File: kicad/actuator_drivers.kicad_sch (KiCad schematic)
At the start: 29 parts, among them J18 Motor 12V, J19 CO2 Solenoid, J20 Chiller, K1 HF46F-12-HS1, K2 HF46F-12-HS1, Q1 IRLZ44NPBF, Q2 IRLZ44NPBF, Q3 2N7002, Q4 2N7002, Q5 IRLZ44NPBF, U10 PC817X1NIP, U11 PC817X1NIP, U3C MCP6002, U7 IR2104SPBF, U8 PC817X2NIP

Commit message: fix: Resolve 5 ERC warnings — footprints, grid alignment, net conflict
1. Inductor footprint: L_4.0x4.0mm_H2.0mm → L_Taiyo-Yuden_NR-40xx
   (power_management.kicad_sch)

2. Relay footprint (×2): Relay_SPST_HF46F → Relay_SPDT_Omron_G5V-1
   (actuator_drivers.kicad_sch — K1, K2)

3. Off-grid coordinates: TPS3823 symbol and WDT_RESET label moved
   from 300.48/310.64 to 300.99/311.15 (1.27mm grid aligned)
   PWR_FLAG reference position 28.575 → 27.94
   (power_management.kicad_sch)

4. HUM_ADC/I2C_SDA overlap: Both hierarchical labels were at same
   coordinates (55.88, 107.95). Shifted I2C_SDA and downstream
   labels down by 2.54mm each to eliminate net conflict.
   (hmi_connectors.kicad_sch)

Co-Authored-By: Devin AI <158243242+devin-ai-integration[bot]@users.noreply.github.com>
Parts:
- K1, K2: footprint Relay_THT:Relay_SPST_HF46F -> Relay_THT:Relay_SPDT_Omron_G5V-1
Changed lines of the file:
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@@
     (property "Reference" "K2" (at 104.14 91.44 0) (effects (font (size 1.27 1.27))))
     (property "Value" "HF46F-12-HS1" (at 104.14 93.98 0) (effects (font (size 1.27 1.27))))
-    (property "Footprint" "Relay_THT:Relay_SPST_HF46F" (at 104.14 101.6 0) (effects (font (size 1.27 1.27)) hide))
+    (property "Footprint" "Relay_THT:Relay_SPDT_Omron_G5V-1" (at 104.14 101.6 0) (effects (font (size 1.27 1.27)) hide))
     (property "MPN" "HF46F-12-HS1" (at 104.14 101.6 0) (effects (font (size 1.27 1.27)) hide))
     (property "Digi-Key_PN" "255-5799-ND" (at 104.14 101.6 0) (effects (font (size 1.27 1.27)) hide))
@@
     (property "Reference" "K1" (at 104.14 129.54 0) (effects (font (size 1.27 1.27))))
     (property "Value" "HF46F-12-HS1" (at 104.14 132.08 0) (effects (font (size 1.27 1.27))))
-    (property "Footprint" "Relay_THT:Relay_SPST_HF46F" (at 104.14 139.7 0) (effects (font (size 1.27 1.27)) hide))
+    (property "Footprint" "Relay_THT:Relay_SPDT_Omron_G5V-1" (at 104.14 139.7 0) (effects (font (size 1.27 1.27)) hide))
     (property "DNP" "Essential,Insight" (at 104.14 139.7 0) (effects (font (size 1.27 1.27)) hide))
     (pin "1") (pin "2")

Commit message: fix: Embed lib_symbols, fix invalid lib_ids, bump to KiCad 9 format
- Embed complete (lib_symbols) definitions in all 5 sub-sheets so symbols
  render as real parts instead of '??' placeholders (files now self-contained)
- Substitute invalid lib_ids with valid library symbols:
  Device:CP -> Device:C_Polarized, Diode:PESD3V3S2USF -> Diode:PESD3V3S1UL,
  Diode:PESD5V0S1BSF -> Diode:PESD5V0S1UL, Isolator:PC817X2 -> Isolator:PC817
- Bump file format version 20231120 -> 20250114 (removes 'older version' warning)
- Left-justify header text blocks so long lines stay within the A3 frame

Validated: kicad-cli SVG render (all real symbols, within frame), clean-room
eeschema GUI render with broken library table (no '??'), and kicad-cli ERC
runs without crashing (425 violations are expected unconnected-pin/dangling-
label items, resolved during per-sheet wiring).

Co-Authored-By: Devin AI <158243242+devin-ai-integration[bot]@users.noreply.github.com>
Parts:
- U8: symbol Isolator:PC817X2 -> Isolator:PC817
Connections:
- new net: K2.5, K2.6
- new net: K1.5, K1.6
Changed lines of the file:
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@@
 (kicad_sch
-  (version 20231120)
+  (version 20250114)
   (generator "devin")
   (generator_version "1.0")
@@
   (text "ACTUATOR DRIVERS — All opto-isolated from MCU\nMotor: IR2104 half-bridge + IRLZ44N MOSFETs (Insight+)\nRelays: PC817 + 2N7002 + HF46F (Insight+/Signature)\nCO2 PWM: RC filter + Op-amp + MOSFET (Insight+)"
     (at 25.4 15.24 0)
-    (effects (font (size 2.54 2.54)))
+    (effects (font (size 2.54 2.54)) (justify left))
   )
   (symbol
-    (lib_id "Isolator:PC817X2")
+    (lib_id "Isolator:PC817")
     (at 63.5 50.8 0) (unit 1)
     (exclude_from_sim no) (in_bom yes) (on_board yes)

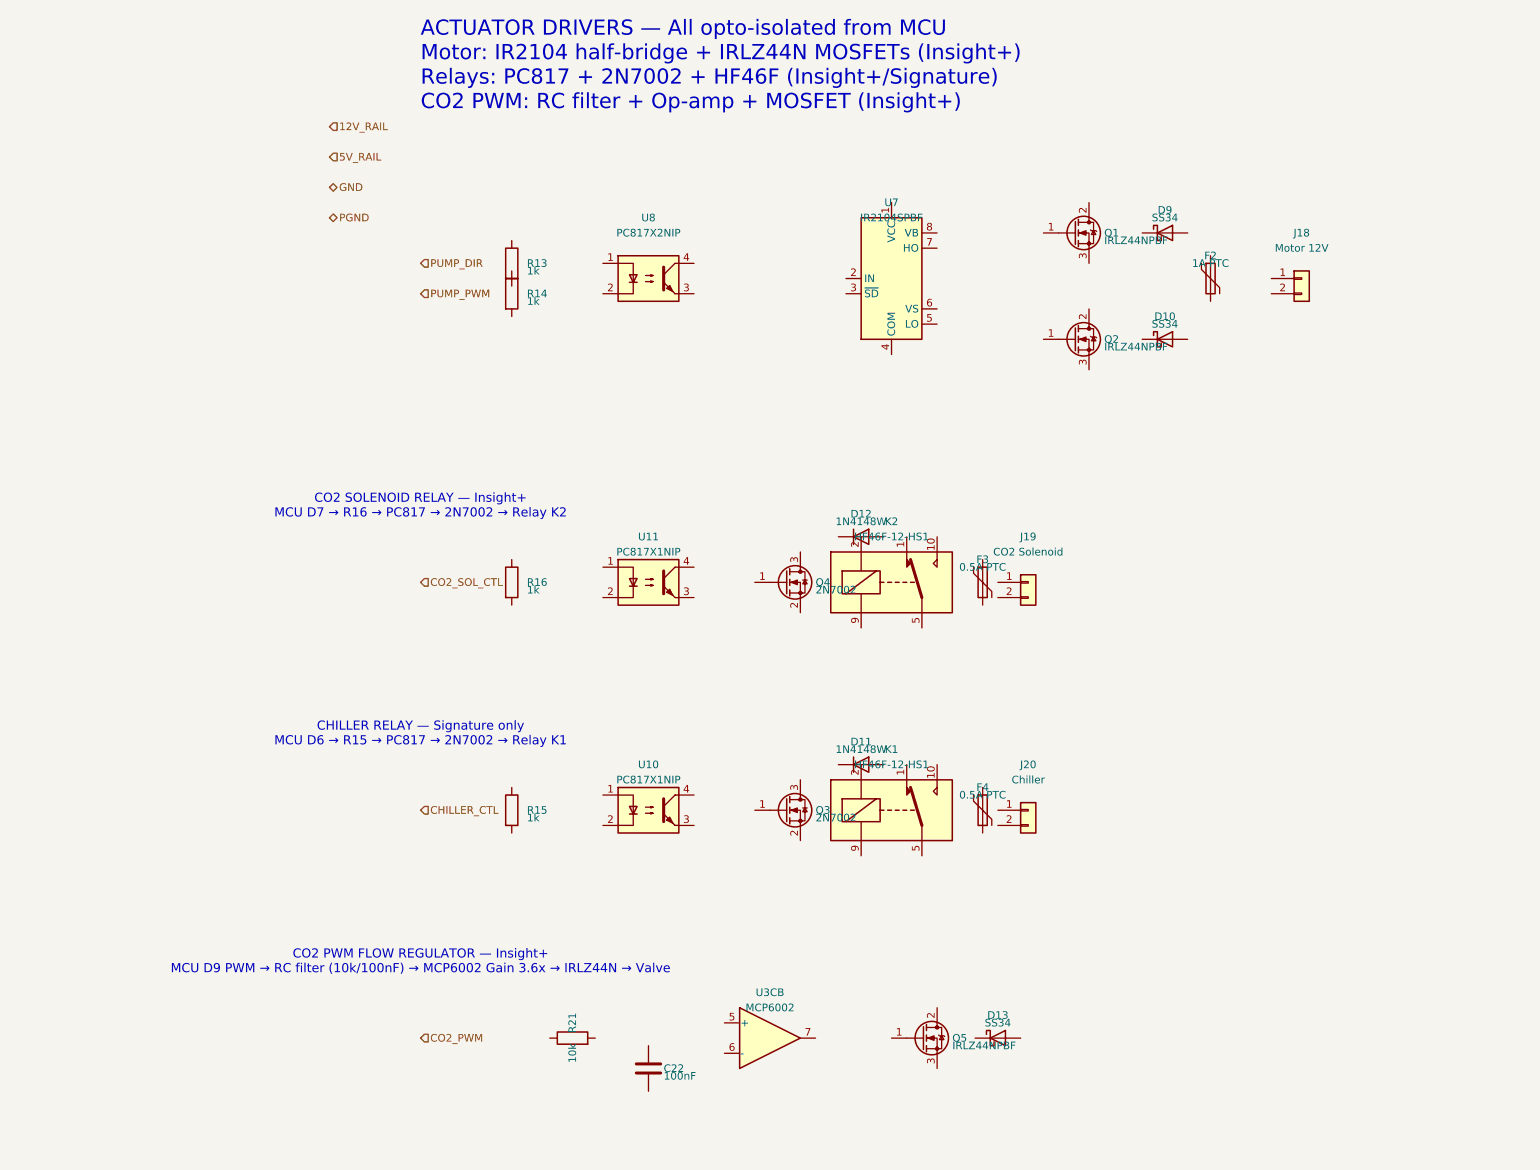
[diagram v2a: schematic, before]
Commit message: fix: Re-annotate components with unique global references + add instances blocks
Root cause: symbol instances lacked (instances ...) blocks, so KiCad treated
all references as unannotated/duplicated (108 duplicate_reference ERC errors)
and produced auto-renamed names (C_DO2, U3_2A, ...) on annotation.

Fix: assign globally-unique sequential standard references (R1..R28, C1..C27,
U1..U20, D1..D18, J1..J21, etc.) and embed a proper (instances) block per
symbol with the correct hierarchical path. Each MCP6002 kept as its own IC
(unit A) to preserve per-channel galvanic isolation (pH/ORP/DO).

ERC: duplicate_reference 108 -> 0, unannotated 1 -> 0.
Co-Authored-By: Devin AI <158243242+devin-ai-integration[bot]@users.noreply.github.com>
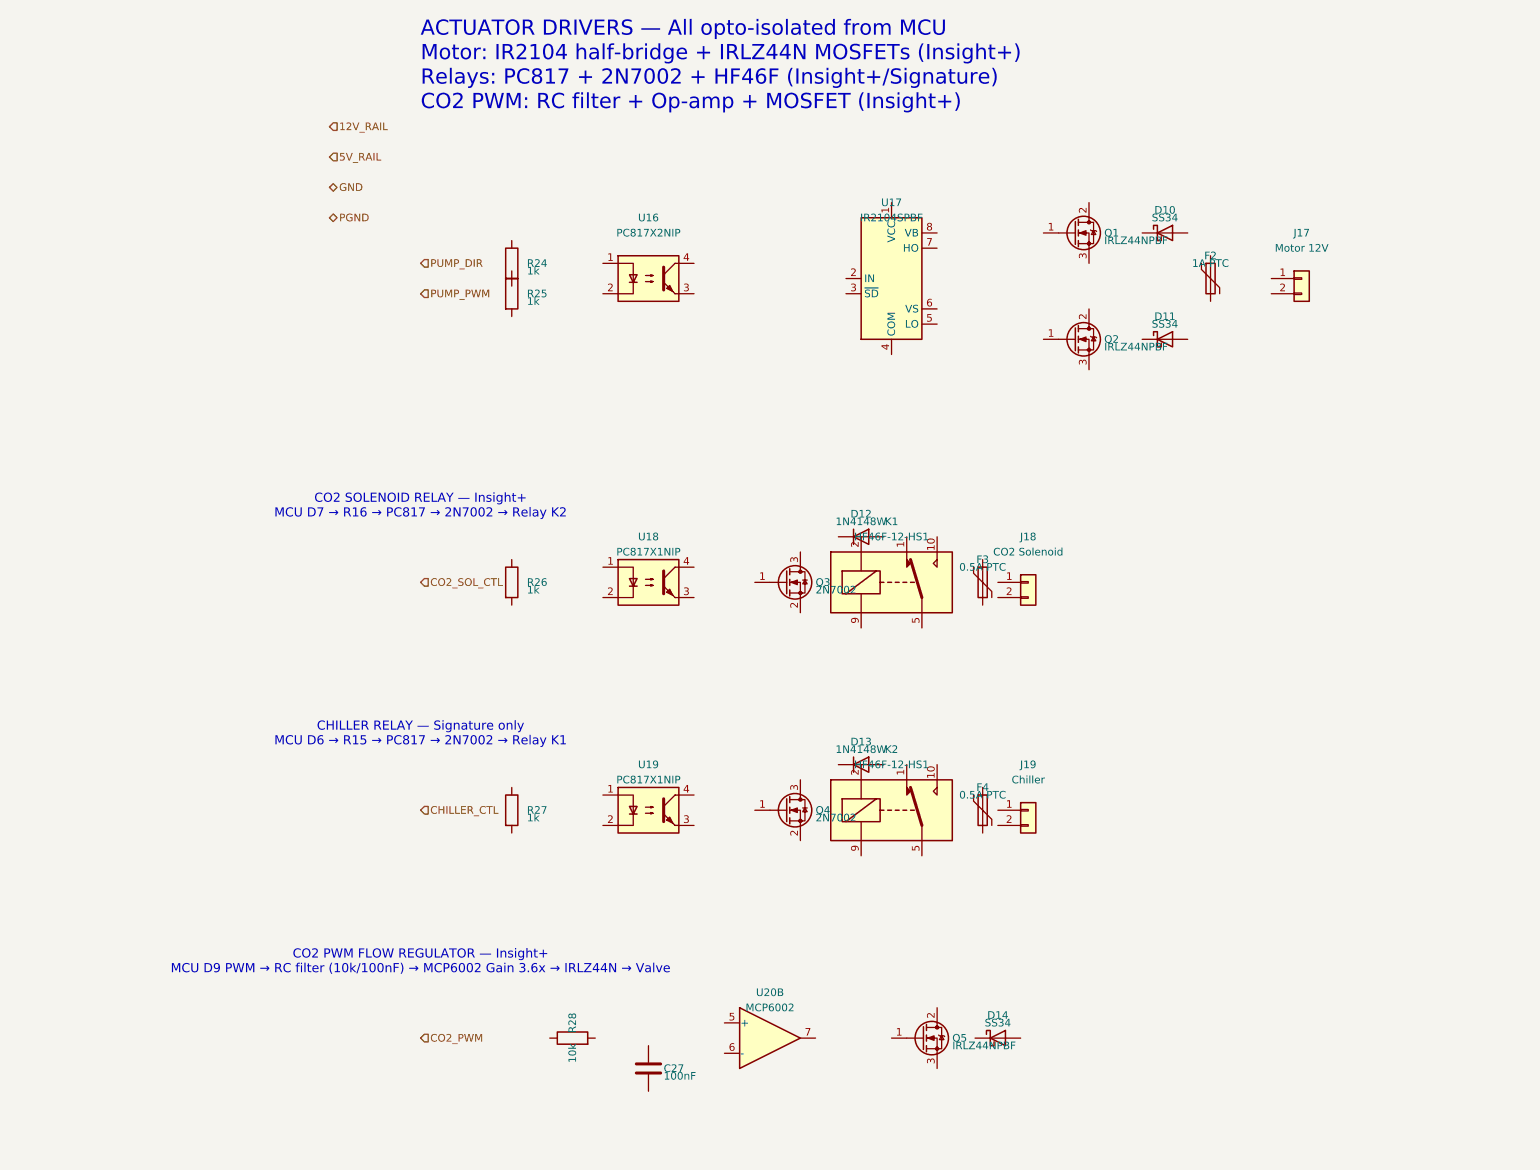
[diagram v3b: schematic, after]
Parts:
- renumbered C22 to C27, D9 to D10, D10 to D11, D11 to D13, D13 to D14, J18 to J17, J19 to J18, J20 to J19, K2 to K1, K1 to K2, Q4 to Q3, Q3 to Q4, R13 to R24, R14 to R25, R16 to R26, R15 to R27, R21 to R28, U8 to U16, U7 to U17, U11 to U18, U10 to U19, U3C to U20

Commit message: fix: reconcile refdes across schematic, BOM, and netlist doc
BOM completely rewritten to match schematic refdes (source of truth):
- U3=TPS3823 (was U12), U4/U7/U10/U11=MCP6002 (was U3 qty2)
- U5/U8/U12=SN6501, U6/U9/U13=AMC1301 (replaces ADuM1250)
- U14=HX711 (was U6), U15=MAX485 (was U13)
- U16=PC817X2, U17=IR2104 (was U7), U18/U19=PC817X1
- R3=WDI pull-up (was R_WDI), R4-R6=LED limits (was R_LED1-3)
- R19/R20=I2C pull-ups (was R10/R11), R21=HX711 pull-up (was R12)
- R24-R27=opto limits (was R13-R20), R28/C27/U20=CO2 PWM (was R21/C22/U3C)
- All connectors shifted: J1=barrel jack, J2-J7=analog, J8-J16=digital
- Added T1-T3, D19-D24, C28-C30 (isolated supply components)

Netlist doc (07_KICAD_NETLIST.md) Rev 2.0:
- All refdes updated to match schematic
- ADC mapping follows firmware: A2=Temp, A3=Hum, A4=CO2, A5=DO
- HX711 on 3V3_RAIL (no level-shift)
- Architecture B2 (AMC1301) documented with isolated supply topology

Schematic additions:
- U21 (ISO1541DR) added to digital_i2c for Atlas EZO I2C isolation
- J22 (Terminal 2P) added to actuator_drivers for CO2 valve output

Co-Authored-By: Devin AI <158243242+devin-ai-integration[bot]@users.noreply.github.com>
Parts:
- added J22: CO2 Valve, Connector_Phoenix_MC:PhoenixContact_MC_1,5_2-G-3.81_1x02_P3.81mm_Horizontal, symbol Connector_Generic:Conn_01x02_Pin
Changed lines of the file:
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@@
   (hierarchical_label "GND"         (shape bidirectional) (at 10.16 35.56 0) (effects (font (size 1.27 1.27))))
   (hierarchical_label "PGND"        (shape bidirectional) (at 10.16 40.64 0) (effects (font (size 1.27 1.27))))
+  (symbol (lib_id "Connector_Generic:Conn_01x02_Pin") (at 139.7 177.8 0) (unit 1) (exclude_from_sim no) (in_bom yes) (on_board yes)
+    (property "Reference" "J22" (at 139.7 172.72 0) (effects (font (size 1.27 1.27))))
+    (property "Value" "CO2 Valve" (at 139.7 175.26 0) (effects (font (size 1.27 1.27))))
+    (property "Footprint" "Connector_Phoenix_MC:PhoenixContact_MC_1,5_2-G-3.81_1x02_P3.81mm_Horizontal" (at 139.7 177.8 0) (effects (font (size 1.27 1.27)) hide))
+    (property "Datasheet" "" (at 139.7 177.8 0) (effects (font (size 1.27 1.27)) hide))
+    (property "MPN" "1757229" (at 139.7 177.8 0) (effects (font (size 1.27 1.27)) hide))
+    (property "Distributor_PN" "277-1273-ND" (at 139.7 177.8 0) (effects (font (size 1.27 1.27)) hide))
+    (instances
+      (project "nebula_qshield"
+        (path "/c6da75fc-541f-4933-b134-f5eb8982a11b/20b0ceca-a23d-4442-9c81-682496868387"
+          (reference "J22") (unit 1)
+        )
+      )
+    )
+  )
 )

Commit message: feat: Wire digital_i2c, actuator_drivers, hmi_connectors + root schematic — ERC violations 322→24 (acceptable)
Co-Authored-By: Devin AI <158243242+devin-ai-integration[bot]@users.noreply.github.com>
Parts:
- added unit 1 of U20
- added unit 3 of U20
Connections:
- net 12V_RAIL: now also D10.1 (K), D12.1 (K), D13.1 (K), D14.1 (K), K1.2, K2.2, Q1.2 (D), U17.1 (VCC), U17.3 (~{SD})
- net 5V_RAIL: now also U20.8 (V+)
- net CHILLER_CTL: now also R27.1
- net CO2_PWM: now also R28.2
- net CO2_SOL_CTL: now also R26.1
- net GND: now also C27.2, R25.2, U16.2, U18.2, U19.2, U20.3 (+), U20.4 (V-)
- net PGND: now also D11.2 (A), J17.2 (Pin_2), J18.2 (Pin_2), J19.2 (Pin_2), Q2.3 (S), Q3.2 (S), Q4.2 (S), Q5.3 (S), U16.3, U17.4 (COM), U18.3, U19.3
- net PUMP_DIR: now also R24.1
- net PUMP_PWM: now also R25.1
- net CHILLER_NO: now reaches F4.1
- net CHILLER_NO: now also K2.10
- net CHILLER_OUT: now reaches F4.2
- net CHILLER_OUT: now also J19.1 (Pin_1), K2.1
- net CHILLER_ISO: now reaches Q4.1 (G)
- net CHILLER_ISO: now also U19.4
- net K2_COIL_N: now reaches Q4.3 (D)
- net K2_COIL_N: now also D13.2 (A), K2.9
- net CO2_SOL_OUT: now reaches K1.1
- net CO2_SOL_OUT: now also F3.2, J18.1 (Pin_1)
- net CO2_SOL_NO: now reaches K1.10
- net CO2_SOL_NO: now also F3.1
- net K1_COIL_N: now reaches K1.9
- net K1_COIL_N: now also D12.2 (A), Q3.3 (D)
- net CO2_PWM_FILT: now reaches R28.1
- net CO2_PWM_FILT: now also C27.1, U20.5 (+)
- net U19_IN: now reaches R27.2
- net U19_IN: now also U19.1
- net U16_INA: now reaches R24.2
- net U16_INA: now also U16.1
- net MOTOR_HO: now reaches Q1.1 (G)
- net MOTOR_HO: now also U17.7 (HO)
- net MOTOR_VS: now reaches Q1.3 (S)
- net MOTOR_VS: now also D10.2 (A), D11.1 (K), F2.1, Q2.2 (D), U17.6 (VS)
- net PUMP_DIR_ISO: now reaches U17.2 (IN)
- net PUMP_DIR_ISO: now also U16.4
- net MOTOR_LO: now reaches U17.5 (LO)
- net MOTOR_LO: now also Q2.1 (G)
- net MOTOR_VB: now reaches U17.8 (VB)
- net MOTOR_VB: now also F2.2, J17.1 (Pin_1)
- net U18_IN: now reaches U18.1
- net U18_IN: now also R26.2
- net CO2_SOL_ISO: now reaches U18.4
- net CO2_SOL_ISO: now also Q3.1 (G)
- net CO2_PWM_OUT: now reaches U20.6 (-)
- net CO2_PWM_OUT: now also Q5.1 (G), U20.7
- net CO2_VALVE: now reaches Q5.2 (D)
- net CO2_VALVE: now also D14.2 (A)
- new net: U20.1, U20.2 (-)
- no-connect marks 0 -> 2
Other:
- note added: "U20 unused sections"
